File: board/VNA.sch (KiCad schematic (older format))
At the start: 66 parts, among them J1 Conn_01x08, J10 Conn_01x01, J11 Conn_01x01, J12 Conn_01x01, J13 Barrel_Jack, J15 Conn_02x05_Odd_Even, J17 Conn_01x04, J18 Conn_01x01, J19 Conn_01x01, J2 Conn_Coaxial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

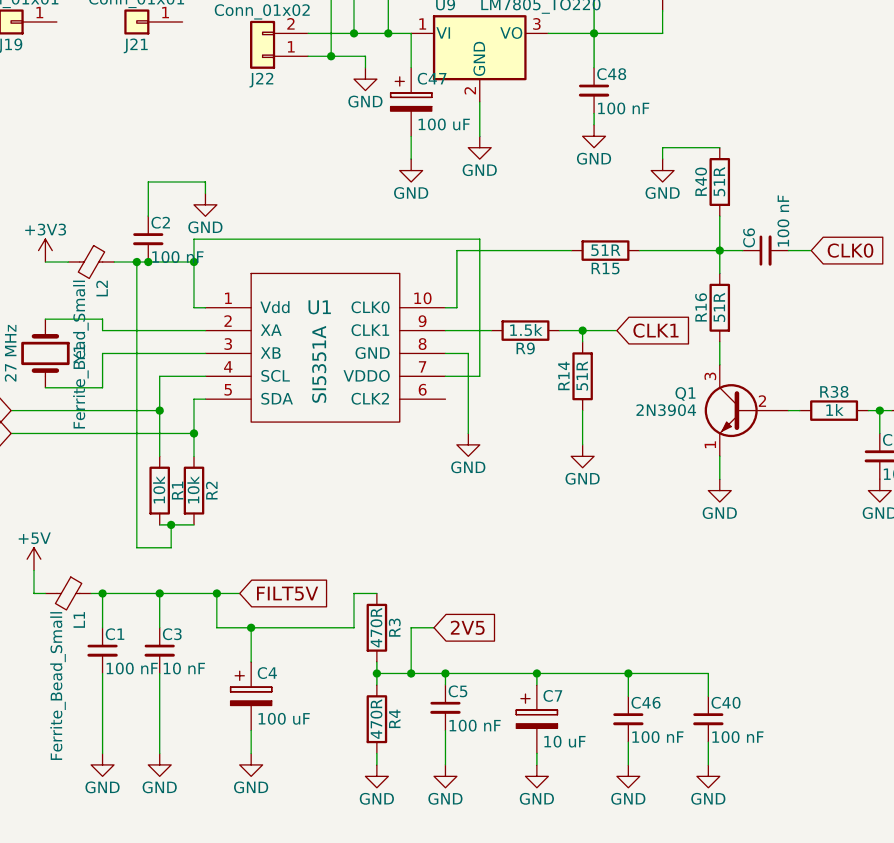
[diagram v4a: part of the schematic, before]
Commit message: Load and Save on Flash
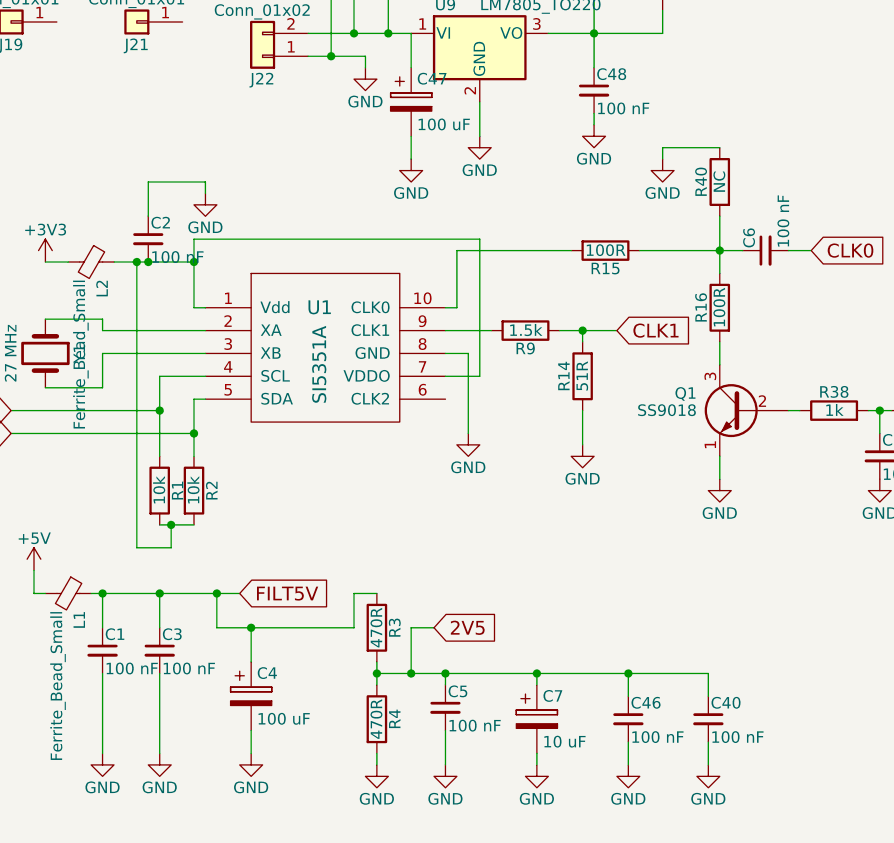
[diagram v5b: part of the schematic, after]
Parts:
- C3: value 10 nF -> 100 nF
- Q1: value 2N3904 -> SS9018
- R15, R16: value 51R -> 100R
- R40: value 51R -> NC
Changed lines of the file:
@@
 P 1600 6350
 F 0 "C3" H 1610 6420 50  0000 L CNN
-F 1 "10 nF" H 1610 6270 50  0000 L CNN
+F 1 "100 nF" H 1610 6270 50  0000 L CNN
 F 2 "Capacitors_THT:C_Disc_D5.0mm_W2.5mm_P2.50mm" H 1600 6350 50  0001 C CNN
 F 3 "" H 1600 6350 50  0001 C CNN
@@
 P 3550 4600
 F 0 "R15" V 3630 4600 50  0000 C CNN
-F 1 "51R" V 3550 4600 50  0000 C CNN
+F 1 "100R" V 3550 4600 50  0000 C CNN
 F 2 "Resistors_THT:R_Axial_DIN0207_L6.3mm_D2.5mm_P7.62mm_Horizontal" V 3480 4600 50  0001 C CNN
 F 3 "" H 3550 4600 50  0001 C CNN
@@
 P 4050 4850
 F 0 "R16" V 4130 4850 50  0000 C CNN
-F 1 "51R" V 4050 4850 50  0000 C CNN
+F 1 "100R" V 4050 4850 50  0000 C CNN
 F 2 "Resistors_THT:R_Axial_DIN0207_L6.3mm_D2.5mm_P7.62mm_Horizontal" V 3980 4850 50  0001 C CNN
 F 3 "" H 4050 4850 50  0001 C CNN
@@
 P 4150 5300
 F 0 "Q1" H 4350 5375 50  0000 L CNN
-F 1 "2N3904" H 4350 5300 50  0000 L CNN
+F 1 "SS9018" H 4350 5300 50  0000 L CNN
 F 2 "TO_SOT_Packages_THT:TO-92_Molded_Narrow" H 4350 5225 50  0001 L CIN
 F 3 "" H 4150 5300 50  0001 L CNN
@@
 P 4050 4300
 F 0 "R40" V 4130 4300 50  0000 C CNN
-F 1 "51R" V 4050 4300 50  0000 C CNN
+F 1 "NC" V 4050 4300 50  0000 C CNN
 F 2 "Resistors_THT:R_Axial_DIN0207_L6.3mm_D2.5mm_P7.62mm_Horizontal" V 3980 4300 50  0001 C CNN
 F 3 "" H 4050 4300 50  0001 C CNN

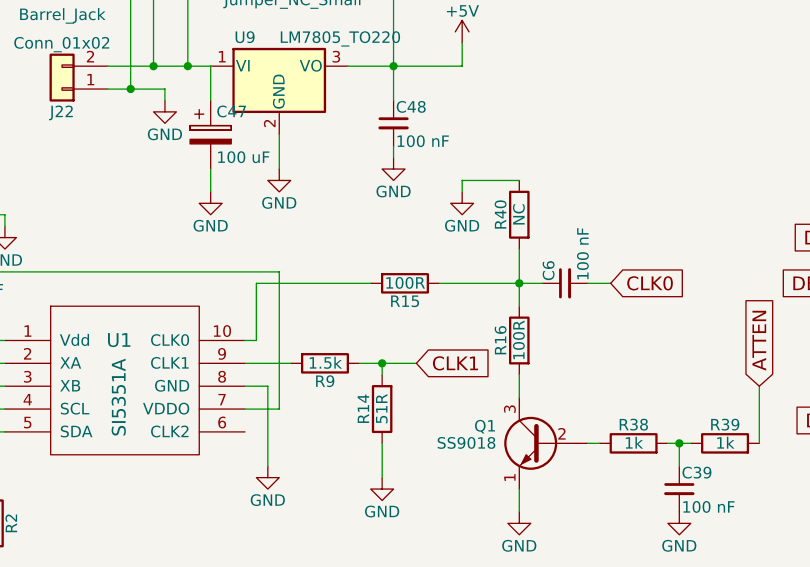
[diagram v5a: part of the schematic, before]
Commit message: Working save to flash, 1 and 2 port, new design
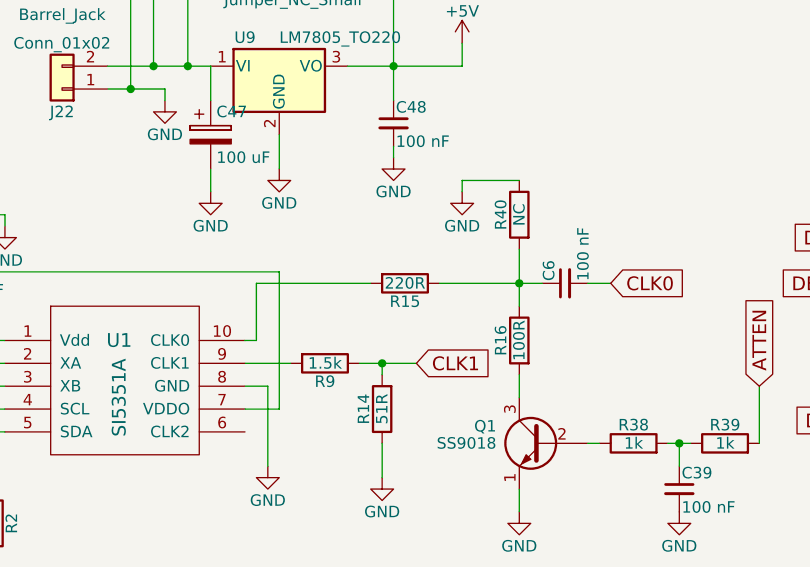
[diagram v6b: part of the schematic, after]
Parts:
- R15: value 100R -> 220R
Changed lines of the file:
@@
 P 3550 4600
 F 0 "R15" V 3630 4600 50  0000 C CNN
-F 1 "100R" V 3550 4600 50  0000 C CNN
+F 1 "220R" V 3550 4600 50  0000 C CNN
 F 2 "Resistors_THT:R_Axial_DIN0207_L6.3mm_D2.5mm_P7.62mm_Horizontal" V 3480 4600 50  0001 C CNN
 F 3 "" H 3550 4600 50  0001 C CNN

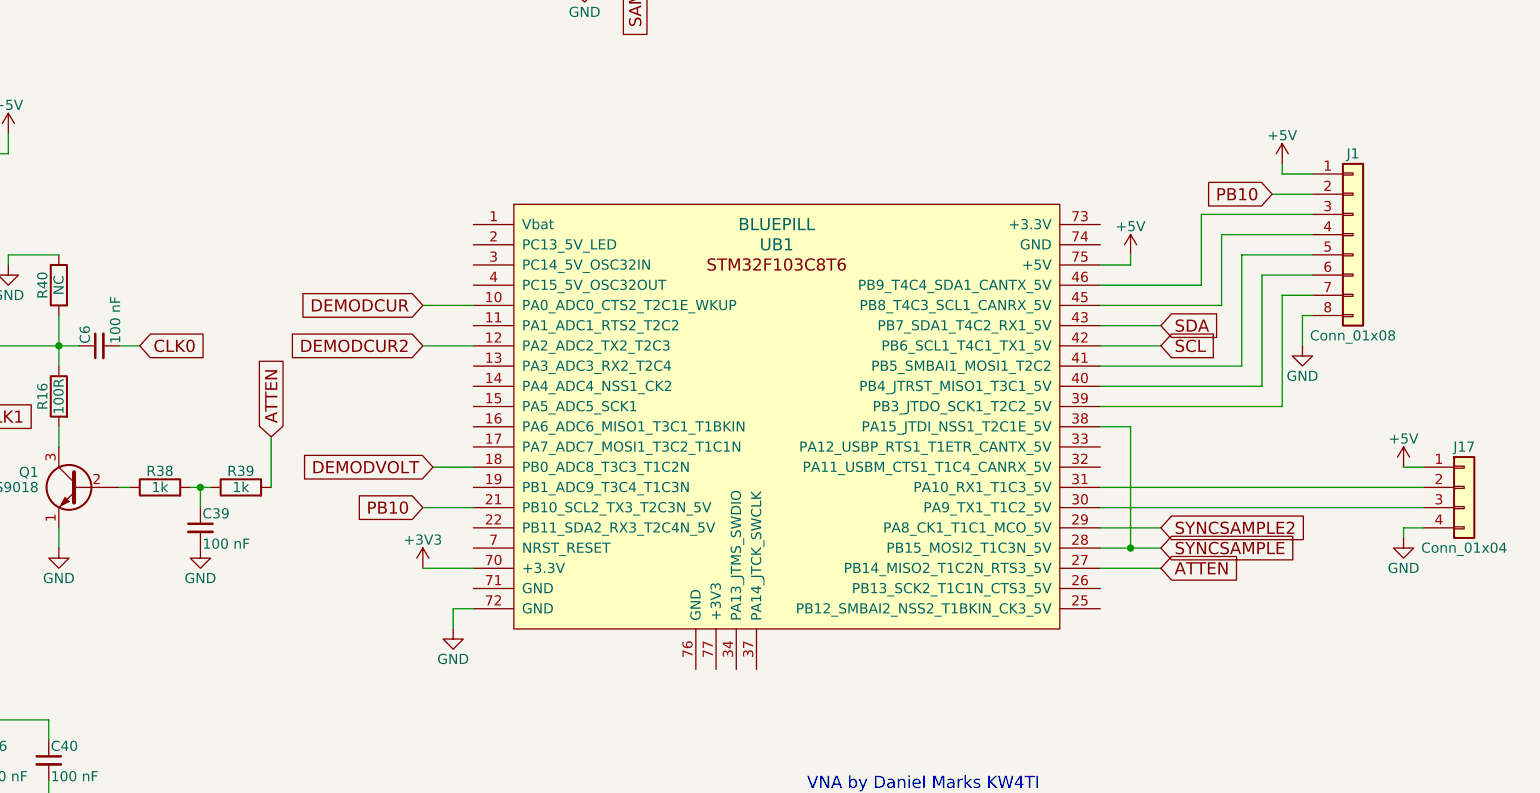
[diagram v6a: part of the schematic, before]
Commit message: Added some more CS pins to header
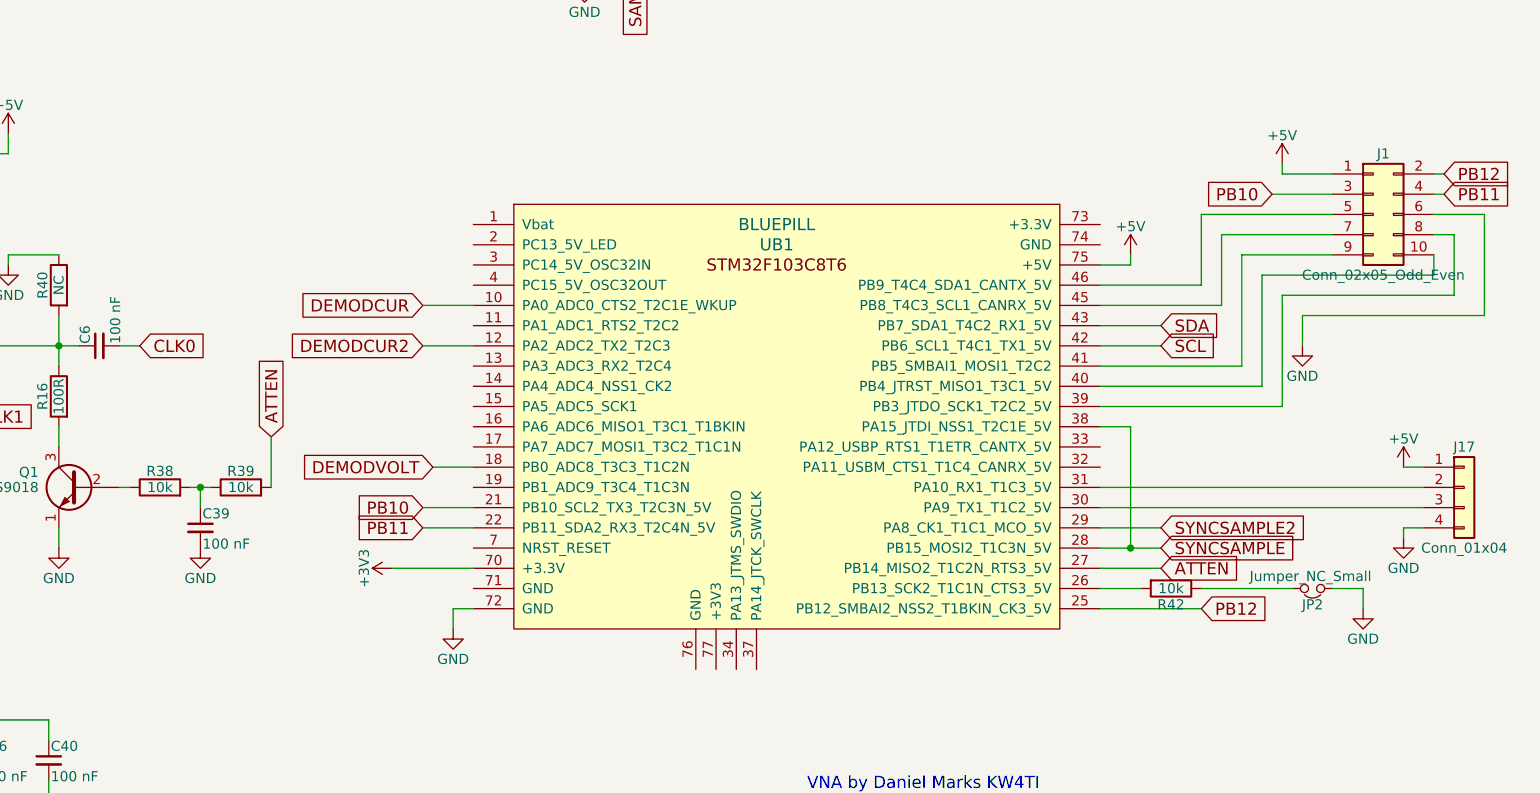
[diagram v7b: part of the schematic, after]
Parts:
- removed J1: Conn_01x08, Pin_Headers:Pin_Header_Straight_1x08_Pitch2.54mm, symbol Conn_01x08
- added J1: Conn_02x05_Odd_Even, Pin_Headers:Pin_Header_Straight_2x05_Pitch2.54mm, symbol Conn_02x05_Odd_Even
- added JP2: Jumper_NC_Small, Pin_Headers:Pin_Header_Straight_1x02_Pitch2.54mm, symbol Jumper_NC_Small
- added R42: 10k, Resistors_THT:R_Axial_DIN0207_L6.3mm_D2.5mm_P7.62mm_Horizontal, symbol R
- R38, R39: value 1k -> 10k
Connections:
- net +5V: now also J1.1 (Pin_1)
- net GND: now also J1.6 (Pin_6), JP2.1
- net PB10: now also J1.3 (Pin_3)
- net PB11: now reaches UB1.22 (PB11_SDA2_RX3_T2C4N_5V)
- net PB11: now also J1.4 (Pin_4)
- net PB12: now reaches UB1.25 (PB12_SMBAI2_NSS2_T1BKIN_CK3_5V)
- net PB12: now also J1.2 (Pin_2)
- net at UB1.26 (PB13_SCK2_T1C1N_CTS3_5V): now also R42.2
- net at UB1.39 (PB3_JTDO_SCK1_T2C2_5V): now also J1.8 (Pin_8)
- net at UB1.40 (PB4_JTRST_MISO1_T3C1_5V): now also J1.10 (Pin_10)
- net at UB1.41 (PB5_SMBAI1_MOSI1_T2C2): now also J1.9 (Pin_9)
- net at UB1.45 (PB8_T4C3_SCL1_CANRX_5V): now also J1.7 (Pin_7)
- net at UB1.46 (PB9_T4C4_SDA1_CANTX_5V): now also J1.5 (Pin_5)
- new net: JP2.2, R42.1
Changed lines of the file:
@@
 L +3V3 #PWR27
 U 1 1 5BB1752D
-P 5850 5700
-F 0 "#PWR27" H 5850 5550 50  0001 C CNN
-F 1 "+3V3" H 5850 5840 50  0000 C CNN
-F 2 "" H 5850 5700 50  0001 C CNN
-F 3 "" H 5850 5700 50  0001 C CNN
-	1    5850 5700
-	1    0    0    -1
+P 5700 5700
+F 0 "#PWR27" H 5700 5550 50  0001 C CNN
+F 1 "+3V3" H 5700 5840 50  0000 C CNN
+F 2 "" H 5700 5700 50  0001 C CNN
+F 3 "" H 5700 5700 50  0001 C CNN
+	1    5700 5700
+	0    -1   -1   0
 $EndComp
 $Comp
@@
 $EndComp
 $Comp
-L +5V #PWR37
+L +5V #PWR38
 U 1 1 5BB3F764
 P 10700 5200
-F 0 "#PWR37" H 10700 5050 50  0001 C CNN
+F 0 "#PWR38" H 10700 5050 50  0001 C CNN
 F 1 "+5V" H 10700 5340 50  0000 C CNN
 F 2 "" H 10700 5200 50  0001 C CNN
@@
 $EndComp
 $Comp
-L GND #PWR38
+L GND #PWR39
 U 1 1 5BB3F96D
 P 10700 5550
-F 0 "#PWR38" H 10700 5300 50  0001 C CNN
+F 0 "#PWR39" H 10700 5300 50  0001 C CNN
 F 1 "GND" H 10700 5400 50  0000 C CNN
 F 2 "" H 10700 5550 50  0001 C CNN
@@
 $EndComp
 $Comp
-L Conn_01x08 J1
-U 1 1 5BB37BFE
-P 10450 4050
-F 0 "J1" H 10450 4450 50  0000 C CNN
-F 1 "Conn_01x08" H 10450 3550 50  0000 C CNN
-F 2 "Pin_Headers:Pin_Header_Straight_1x08_Pitch2.54mm" H 10450 4050 50  0001 C CNN
-F 3 "" H 10450 4050 50  0001 C CNN
-	1    10450 4050
-	1    0    0    -1
-$EndComp
-$Comp
 L GND #PWR34
 U 1 1 5BB37FFB
@@
 PB10
 $Comp
-L +3V3 #PWR36
+L +3V3 #PWR37
 U 1 1 5BB22189
 P 10550 1600
-F 0 "#PWR36" H 10550 1450 50  0001 C CNN
+F 0 "#PWR37" H 10550 1450 50  0001 C CNN
 F 1 "+3V3" H 10550 1740 50  0000 C CNN
 F 2 "" H 10550 1600 50  0001 C CNN
@@
 $EndComp
 $Comp
-L GND #PWR35
+L GND #PWR36
 U 1 1 5BE3A08F
 P 10350 2000
-F 0 "#PWR35" H 10350 1750 50  0001 C CNN
+F 0 "#PWR36" H 10350 1750 50  0001 C CNN
 F 1 "GND" H 10350 1850 50  0000 C CNN
 F 2 "" H 10350 2000 50  0001 C CNN
@@
 P 4550 5300
 F 0 "R38" V 4630 5300 50  0000 C CNN
-F 1 "1k" V 4550 5300 50  0000 C CNN
+F 1 "10k" V 4550 5300 50  0000 C CNN
 F 2 "Resistors_THT:R_Axial_DIN0207_L6.3mm_D2.5mm_P7.62mm_Horizontal" V 4480 5300 50  0001 C CNN
 F 3 "" H 4550 5300 50  0001 C CNN
@@
 P 4950 5300
 F 0 "R39" V 5030 5300 50  0000 C CNN
-F 1 "1k" V 4950 5300 50  0000 C CNN
+F 1 "10k" V 4950 5300 50  0000 C CNN
 F 2 "Resistors_THT:R_Axial_DIN0207_L6.3mm_D2.5mm_P7.62mm_Horizontal" V 4880 5300 50  0001 C CNN
 F 3 "" H 4950 5300 50  0001 C CNN
@@
 	9250 1300 9600 1300
 Wire Wire Line
-	10250 3850 10050 3850
+	10050 3850 10350 3850
 Wire Wire Line
 	5850 5400 6100 5400
@@
 	2600 3650 2600 3300
 Wire Wire Line
-	10100 3750 10250 3750
+	10100 3750 10350 3750
 Wire Wire Line
 	10100 3700 10100 3750
 Wire Wire Line
-	10200 4450 10250 4450
+	10200 4450 11100 4450
 Wire Wire Line
 	10200 4600 10200 4450
 Wire Wire Line
-	9700 3950 10250 3950
+	9700 3950 10350 3950
 Wire Wire Line
 	9700 4300 9700 3950
@@
 	9200 4300 9700 4300
 Wire Wire Line
-	9800 4050 10250 4050
+	9800 4050 10350 4050
 Wire Wire Line
 	9800 4400 9800 4050
@@
 	9200 4400 9800 4400
 Wire Wire Line
-	10100 4350 10250 4350
+	10100 4350 10950 4350
 Wire Wire Line
 	10100 4900 10100 4350
@@
 	9200 4900 10100 4900
 Wire Wire Line
-	10000 4250 10250 4250
+	10000 4250 10850 4250
 Wire Wire Line
 	10000 4800 10000 4250
@@
 	9200 4800 10000 4800
 Wire Wire Line
-	9900 4150 10250 4150
+	9900 4150 10350 4150
 Wire Wire Line
 	9900 4700 9900 4150
@@
 	4950 2150 4950 2300
 Wire Wire Line
-	6100 5700 5850 5700
+	5700 5700 6100 5700
 Wire Wire Line
 	6000 5900 6100 5900
@@
 	4000 6450 4000 6550
 Connection ~ 3650 6450
+$Comp
+L Jumper_NC_Small JP2
+U 1 1 5C1BD083
+P 10250 5800
+F 0 "JP2" H 10250 5880 50  0000 C CNN
+F 1 "Jumper_NC_Small" H 10260 5740 50  0000 C CNN
+F 2 "Pin_Headers:Pin_Header_Straight_1x02_Pitch2.54mm" H 10250 5800 50  0001 C CNN
+F 3 "" H 10250 5800 50  0001 C CNN
+	1    10250 5800
+	-1   0    0    1
+$EndComp
+$Comp
+L R R42
+U 1 1 5C1BD47E
+P 9550 5800
+F 0 "R42" V 9630 5800 50  0000 C CNN
+F 1 " 10k" V 9550 5800 50  0000 C CNN
+F 2 "Resistors_THT:R_Axial_DIN0207_L6.3mm_D2.5mm_P7.62mm_Horizontal" V 9480 5800 50  0001 C CNN
+F 3 "" H 9550 5800 50  0001 C CNN
+	1    9550 5800
+	0    1    1    0
+$EndComp
+Wire Wire Line
+	9200 5900 9700 5900
+Wire Wire Line
+	9700 5800 10150 5800
+$Comp
+L GND #PWR35
+U 1 1 5C1BDCBD
+P 10500 5900
+F 0 "#PWR35" H 10500 5650 50  0001 C CNN
+F 1 "GND" H 10500 5750 50  0000 C CNN
+F 2 "" H 10500 5900 50  0001 C CNN
+F 3 "" H 10500 5900 50  0001 C CNN
+	1    10500 5900
+	1    0    0    -1
+$EndComp
+Wire Wire Line
+	10350 5800 10500 5800
+Wire Wire Line
+	10500 5800 10500 5900
+$Comp
+L Conn_02x05_Odd_Even J1
+U 1 1 5C1BEA55
+P 10550 3950
+F 0 "J1" H 10600 4250 50  0000 C CNN
+F 1 "Conn_02x05_Odd_Even" H 10600 3650 50  0000 C CNN
+F 2 "Pin_Headers:Pin_Header_Straight_2x05_Pitch2.54mm" H 10550 3950 50  0001 C CNN
+F 3 "" H 10550 3950 50  0001 C CNN
+	1    10550 3950
+	1    0    0    -1
+$EndComp
+Wire Wire Line
+	10850 4250 10850 4150
+Wire Wire Line
+	10950 4350 10950 4050
+Wire Wire Line
+	10950 4050 10850 4050
+Wire Wire Line
+	11100 4450 11100 3950
+Wire Wire Line
+	11100 3950 10850 3950
+Text GLabel 5850 5500 0    60   Input ~ 0
+PB11
+Wire Wire Line
+	5850 5500 6100 5500
+Text GLabel 10900 3850 2    60   Input ~ 0
+PB11
+Wire Wire Line
+	10900 3850 10850 3850
+Wire Wire Line
+	9400 5800 9200 5800
+Text GLabel 9700 5900 2    60   Input ~ 0
+PB12
+Text GLabel 10900 3750 2    60   Input ~ 0
+PB12
+Wire Wire Line
+	10900 3750 10850 3750
 $EndSCHEMATC

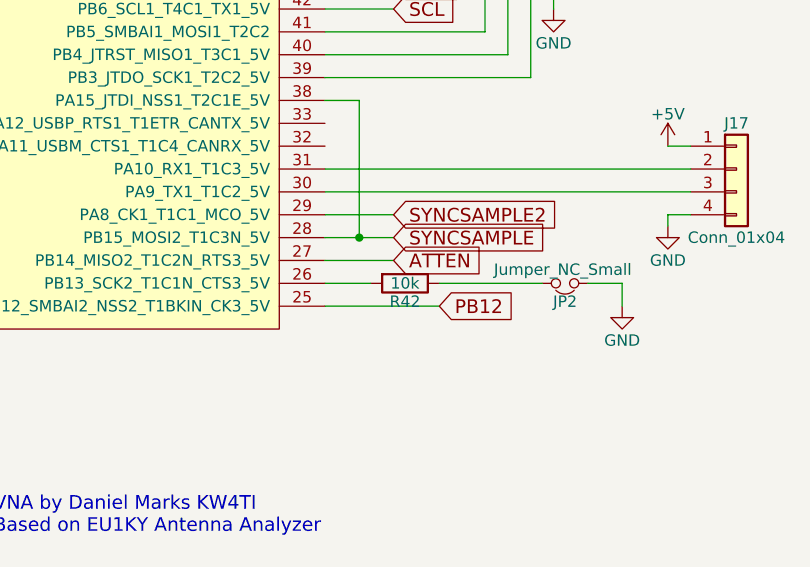
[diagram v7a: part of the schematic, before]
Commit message: Added Smith Chart plot
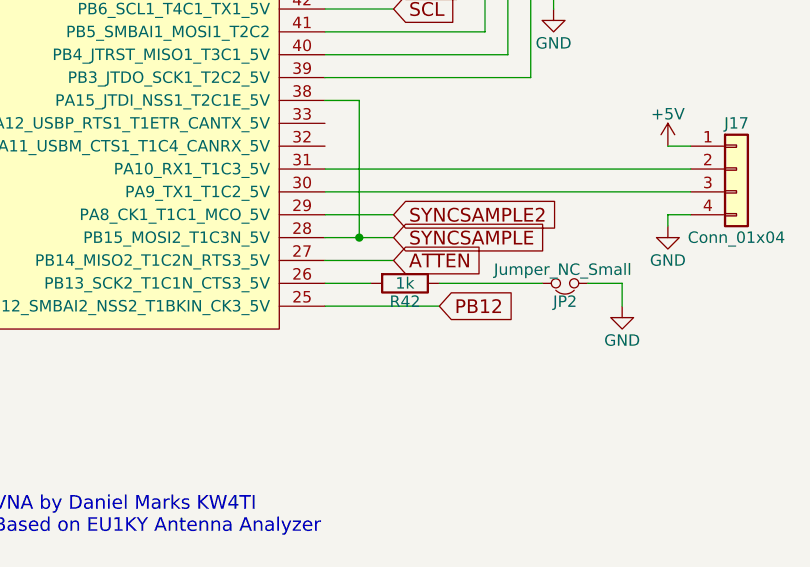
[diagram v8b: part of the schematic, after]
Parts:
- R42: value 10k -> 1k
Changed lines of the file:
@@
 P 9550 5800
 F 0 "R42" V 9630 5800 50  0000 C CNN
-F 1 " 10k" V 9550 5800 50  0000 C CNN
+F 1 "1k" V 9550 5800 50  0000 C CNN
 F 2 "Resistors_THT:R_Axial_DIN0207_L6.3mm_D2.5mm_P7.62mm_Horizontal" V 9480 5800 50  0001 C CNN
 F 3 "" H 9550 5800 50  0001 C CNN
